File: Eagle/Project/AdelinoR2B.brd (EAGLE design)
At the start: 47 x 53.3 mm, 68 parts, among them J1 DC-044-A, J2 YELLOW-8P-2.54, J3 YELLOW-6P-2.54, J4 YELLOW-8P-2.54, J5 YELLOW-8P-2.54, J6 4P-2.0, J7 YELLOW-2X3P-2.54, J8 4P-2.0, Q1 NCE3407A, Q2 CJ2305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

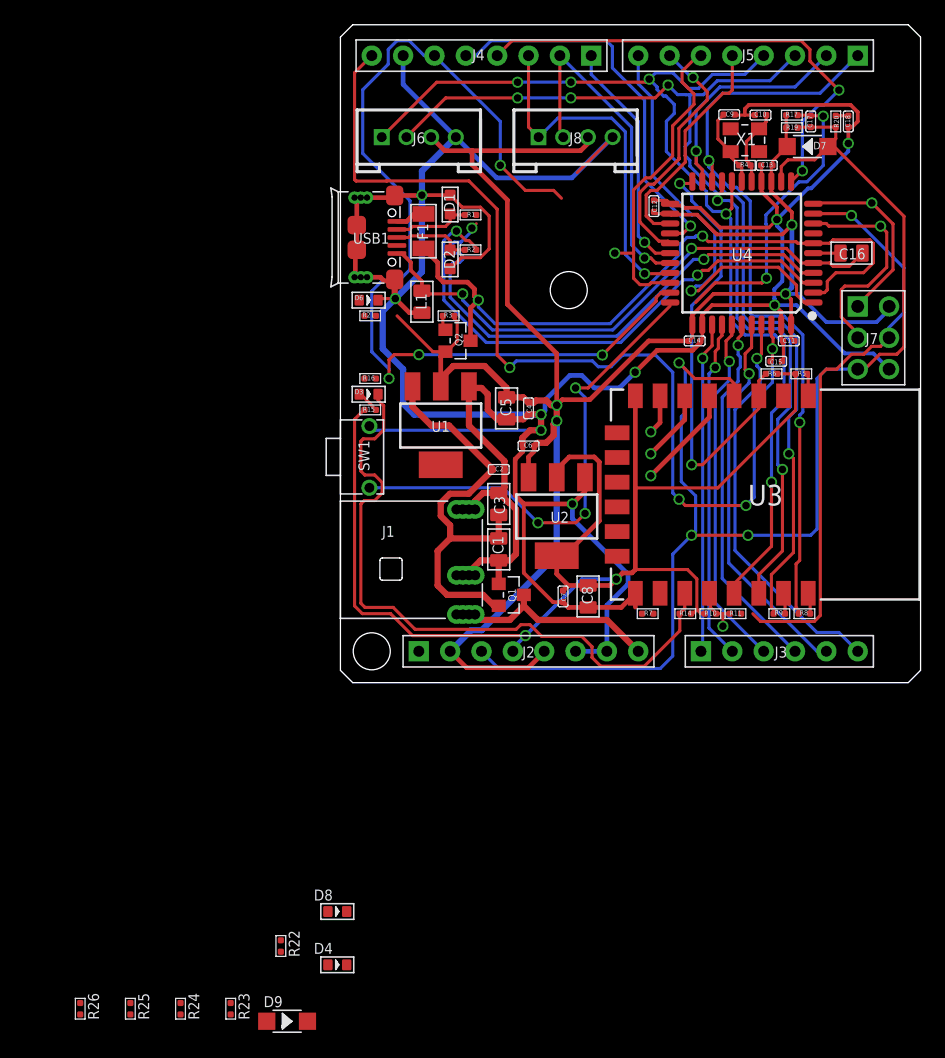
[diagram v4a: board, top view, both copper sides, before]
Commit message: Reserve resistor for GPIO16/RESET.
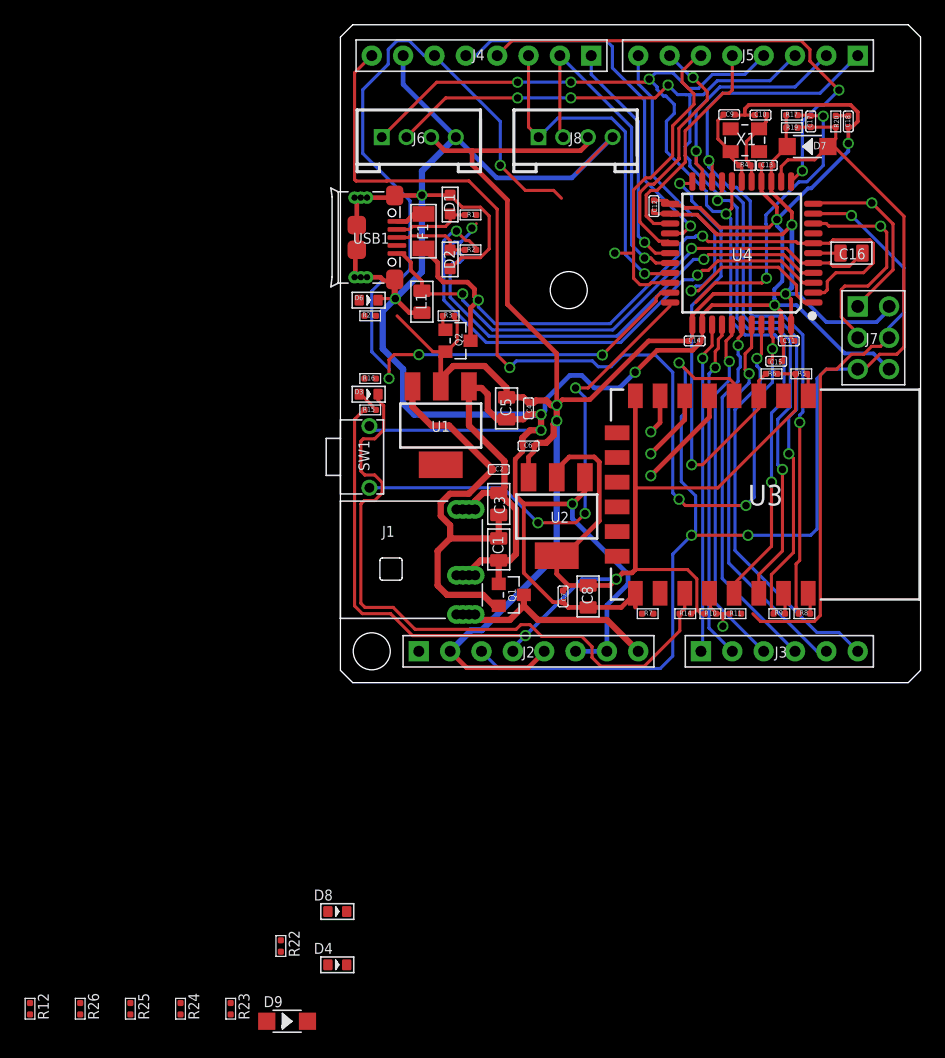
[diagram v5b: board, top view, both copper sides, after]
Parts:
- added R12: 0R, Seeed-Resistor:R0402
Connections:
- new net N$11: R12.2, U3.4
- net RESET: now also R12.1; no longer U3.4
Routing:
- net RESET: track 108.4 -> 107.4 mm
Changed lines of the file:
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@@
 <element name="C10" library="Seeed-Capacitor" package="C0402" value="22pf" x="34.036" y="45.9835" smashed="yes" rot="R90">
 <attribute name="MPN" value="CC0402JRNPO9BN220" x="34.036" y="45.9835" size="1.778" layer="27" rot="R90" display="off"/>
+<attribute name="NAME" x="33.528" y="45.8565" size="0.4064" layer="25" ratio="11"/>
 <attribute name="NAME" x="32.766" y="45.7295" size="0.635" layer="33" ratio="10"/>
-<attribute name="NAME" x="33.528" y="45.8565" size="0.4064" layer="25" ratio="11"/>
 <attribute name="VALUE" x="32.766" y="44.396" size="0.635" layer="27" ratio="10"/>
 </element>
@@
 <element name="C9" library="Seeed-Capacitor" package="C0402" value="22pf" x="31.496" y="46.0195" smashed="yes" rot="R270">
 <attribute name="MPN" value="CC0402JRNPO9BN220" x="31.496" y="46.0195" size="1.778" layer="27" rot="R270" display="off"/>
+<attribute name="NAME" x="31.877" y="46.2735" size="0.4064" layer="25" ratio="11" rot="R180"/>
 <attribute name="NAME" x="32.766" y="46.2735" size="0.635" layer="33" ratio="10" rot="R180"/>
-<attribute name="NAME" x="31.877" y="46.2735" size="0.4064" layer="25" ratio="11" rot="R180"/>
 <attribute name="VALUE" x="32.766" y="47.607" size="0.635" layer="27" ratio="10" rot="R180"/>
 </element>
@@
 <element name="J1" library="Seeed-Connector" package="DCJ3P-11.6X9.6X7.0MM" value="DC-044-A" x="0" y="9.906" smashed="yes" rot="R270">
 <attribute name="MPN" value="JACK-DC-044-A" x="0" y="9.906" size="1.778" layer="27" rot="R270" display="off"/>
+<attribute name="NAME" x="3.3655" y="11.811" size="0.889" layer="25" ratio="11"/>
 <attribute name="NAME" x="6.985" y="13.1445" size="1.27" layer="33" ratio="10" rot="R270"/>
-<attribute name="NAME" x="3.3655" y="11.811" size="0.889" layer="25" ratio="11"/>
 <attribute name="VALUE" x="4.3815" y="3.556" size="0.889" layer="27" ratio="11"/>
 </element>
 <element name="J3" library="Seeed-Connector" package="H6-2.54" value="YELLOW-6P-2.54" x="35.56" y="2.54" smashed="yes" rot="R90">
 <attribute name="MPN" value="F185-1106A1BSYA3" x="35.56" y="2.54" size="1.778" layer="27" rot="R90" display="off"/>
+<attribute name="NAME" x="36.195" y="2.921" size="0.889" layer="25" ratio="11" rot="R180"/>
 <attribute name="NAME" x="38.1" y="3.175" size="0.635" layer="33" ratio="10" rot="R180"/>
-<attribute name="NAME" x="36.195" y="2.921" size="0.889" layer="25" ratio="11" rot="R180"/>
 <attribute name="VALUE" x="37.465" y="5.08" size="0.889" layer="27" ratio="11" rot="R180"/>
 </element>
 <element name="J2" library="Seeed-Connector" package="H8-2.54" value="YELLOW-8P-2.54" x="15.24" y="2.54" smashed="yes" rot="R90">
 <attribute name="MPN" value="F185-1108A1BSYC1" x="15.24" y="2.54" size="1.778" layer="27" rot="R90" display="off"/>
+<attribute name="NAME" x="15.748" y="2.921" size="0.889" layer="25" ratio="11" rot="R180"/>
 <attribute name="NAME" x="15.875" y="2.54" size="0.3048" layer="33" ratio="10" rot="R180"/>
-<attribute name="NAME" x="15.748" y="2.921" size="0.889" layer="25" ratio="11" rot="R180"/>
 <attribute name="VALUE" x="16.51" y="5.08" size="0.889" layer="27" ratio="11" rot="R180"/>
 </element>
 <element name="J5" library="Seeed-Connector" package="H8-2.54" value="YELLOW-8P-2.54" x="33.02" y="50.8" smashed="yes" rot="R270">
 <attribute name="MPN" value="F185-1108A1BSYC1" x="33.02" y="50.8" size="1.778" layer="27" rot="R270" display="off"/>
+<attribute name="NAME" x="32.512" y="50.419" size="0.889" layer="25" ratio="11"/>
 <attribute name="NAME" x="32.385" y="50.8" size="0.3048" layer="33" ratio="10"/>
-<attribute name="NAME" x="32.512" y="50.419" size="0.889" layer="25" ratio="11"/>
 <attribute name="VALUE" x="31.75" y="48.26" size="0.889" layer="27" ratio="11"/>
 </element>
 <element name="J4" library="Seeed-Connector" package="H8-2.54" value="YELLOW-8P-2.54" x="11.43" y="50.8" smashed="yes" rot="R270">
 <attribute name="MPN" value="F185-1108A1BSYC1" x="11.43" y="50.8" size="1.778" layer="27" rot="R270" display="off"/>
+<attribute name="NAME" x="10.668" y="50.419" size="0.889" layer="25" ratio="11"/>
 <attribute name="NAME" x="10.795" y="50.8" size="0.3048" layer="33" ratio="10"/>
-<attribute name="NAME" x="10.668" y="50.419" size="0.889" layer="25" ratio="11"/>
 <attribute name="VALUE" x="10.16" y="48.26" size="0.889" layer="27" ratio="11"/>
 </element>
@@
 <element name="D9" library="Seeed-Diode" package="SOD-123" value="20V-500MA" x="-4.318" y="-27.432" smashed="yes">
 <attribute name="MPN" value="MBR0520LT1G" x="-4.318" y="-27.432" size="1.778" layer="27" display="off"/>
+<attribute name="NAME" x="-5.207" y="-28.067" size="0.381" layer="33" ratio="10"/>
 <attribute name="NAME" x="-6.223" y="-26.289" size="0.889" layer="25" ratio="11"/>
-<attribute name="NAME" x="-5.207" y="-28.067" size="0.381" layer="33" ratio="10"/>
 <attribute name="VALUE" x="-6.223" y="-29.464" size="0.889" layer="27" font="vector" ratio="11"/>
 </element>
@@
 <attribute name="NAME" x="-20.447" y="-25.146" size="0.889" layer="25" ratio="11" rot="R270"/>
 <attribute name="VALUE" x="-22.606" y="-25.146" size="0.889" layer="27" font="vector" ratio="11" rot="R270"/>
+</element>
+<element name="R12" library="Seeed-Resistor" package="R0402" value="0R" x="-25.146" y="-26.416" smashed="yes">
+<attribute name="MPN" value="RC0402JR-070RL" x="-25.146" y="-26.416" size="1.778" layer="27" display="off"/>
+<attribute name="NAME" x="-24.511" y="-25.146" size="0.889" layer="25" ratio="11" rot="R270"/>
+<attribute name="VALUE" x="-26.67" y="-25.146" size="0.889" layer="27" font="vector" ratio="11" rot="R270"/>
 </element>
 </elements>
@@
 <wire x1="43.69625" y1="26.6065" x2="42.48975" y2="25.4" width="0.254" layer="1"/>
 <wire x1="45.6565" y1="27.18625" x2="45.07675" y2="26.6065" width="0.254" layer="1"/>
-<contactref element="U3" pad="4"/>
 <wire x1="27.94" y1="25.4" x2="27.432" y2="25.908" width="0.254" layer="16"/>
 <via x="27.432" y="25.908" extent="1-16" drill="0.6096"/>
@@
 <wire x1="28.702" y1="24.638" x2="31.496" y2="24.638" width="0.254" layer="1"/>
 <wire x1="31.496" y1="24.638" x2="31.897" y2="24.237" width="0.254" layer="1"/>
-<wire x1="31.897" y1="24.237" x2="31.897" y2="23.24" width="0.254" layer="1"/>
+<contactref element="R12" pad="1"/>
+<wire x1="11.43" y1="2.54" x2="-25.146" y2="-25.9535" width="0" layer="19" extent="1-1"/>
 </signal>
 <signal name="PIN_AREF">
@@
 <wire x1="-1.016" y1="-22.86" x2="2.8755" y2="24.638" width="0" layer="19" extent="1-1"/>
 </signal>
+<signal name="N$11">
+<contactref element="U3" pad="4"/>
+<contactref element="R12" pad="2"/>
+<wire x1="-25.146" y1="-26.8785" x2="31.897" y2="23.24" width="0" layer="19" extent="1-1"/>
+</signal>
 </signals>

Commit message: Wip.
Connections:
- net +5V: no longer R16.1
- net GND: now also D4.-
- net PIN_D13: now also R16.1; no longer D4.-
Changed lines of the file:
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@@
 <element name="C10" library="Seeed-Capacitor" package="C0402" value="22pf" x="34.036" y="45.9835" smashed="yes" rot="R90">
 <attribute name="MPN" value="CC0402JRNPO9BN220" x="34.036" y="45.9835" size="1.778" layer="27" rot="R90" display="off"/>
+<attribute name="NAME" x="32.766" y="45.7295" size="0.635" layer="33" ratio="10"/>
 <attribute name="NAME" x="33.528" y="45.8565" size="0.4064" layer="25" ratio="11"/>
-<attribute name="NAME" x="32.766" y="45.7295" size="0.635" layer="33" ratio="10"/>
 <attribute name="VALUE" x="32.766" y="44.396" size="0.635" layer="27" ratio="10"/>
 </element>
@@
 <element name="C9" library="Seeed-Capacitor" package="C0402" value="22pf" x="31.496" y="46.0195" smashed="yes" rot="R270">
 <attribute name="MPN" value="CC0402JRNPO9BN220" x="31.496" y="46.0195" size="1.778" layer="27" rot="R270" display="off"/>
+<attribute name="NAME" x="32.766" y="46.2735" size="0.635" layer="33" ratio="10" rot="R180"/>
 <attribute name="NAME" x="31.877" y="46.2735" size="0.4064" layer="25" ratio="11" rot="R180"/>
-<attribute name="NAME" x="32.766" y="46.2735" size="0.635" layer="33" ratio="10" rot="R180"/>
 <attribute name="VALUE" x="32.766" y="47.607" size="0.635" layer="27" ratio="10" rot="R180"/>
 </element>
@@
 <element name="J1" library="Seeed-Connector" package="DCJ3P-11.6X9.6X7.0MM" value="DC-044-A" x="0" y="9.906" smashed="yes" rot="R270">
 <attribute name="MPN" value="JACK-DC-044-A" x="0" y="9.906" size="1.778" layer="27" rot="R270" display="off"/>
+<attribute name="NAME" x="6.985" y="13.1445" size="1.27" layer="33" ratio="10" rot="R270"/>
 <attribute name="NAME" x="3.3655" y="11.811" size="0.889" layer="25" ratio="11"/>
-<attribute name="NAME" x="6.985" y="13.1445" size="1.27" layer="33" ratio="10" rot="R270"/>
 <attribute name="VALUE" x="4.3815" y="3.556" size="0.889" layer="27" ratio="11"/>
 </element>
 <element name="J3" library="Seeed-Connector" package="H6-2.54" value="YELLOW-6P-2.54" x="35.56" y="2.54" smashed="yes" rot="R90">
 <attribute name="MPN" value="F185-1106A1BSYA3" x="35.56" y="2.54" size="1.778" layer="27" rot="R90" display="off"/>
+<attribute name="NAME" x="38.1" y="3.175" size="0.635" layer="33" ratio="10" rot="R180"/>
 <attribute name="NAME" x="36.195" y="2.921" size="0.889" layer="25" ratio="11" rot="R180"/>
-<attribute name="NAME" x="38.1" y="3.175" size="0.635" layer="33" ratio="10" rot="R180"/>
 <attribute name="VALUE" x="37.465" y="5.08" size="0.889" layer="27" ratio="11" rot="R180"/>
 </element>
 <element name="J2" library="Seeed-Connector" package="H8-2.54" value="YELLOW-8P-2.54" x="15.24" y="2.54" smashed="yes" rot="R90">
 <attribute name="MPN" value="F185-1108A1BSYC1" x="15.24" y="2.54" size="1.778" layer="27" rot="R90" display="off"/>
+<attribute name="NAME" x="15.875" y="2.54" size="0.3048" layer="33" ratio="10" rot="R180"/>
 <attribute name="NAME" x="15.748" y="2.921" size="0.889" layer="25" ratio="11" rot="R180"/>
-<attribute name="NAME" x="15.875" y="2.54" size="0.3048" layer="33" ratio="10" rot="R180"/>
 <attribute name="VALUE" x="16.51" y="5.08" size="0.889" layer="27" ratio="11" rot="R180"/>
 </element>
 <element name="J5" library="Seeed-Connector" package="H8-2.54" value="YELLOW-8P-2.54" x="33.02" y="50.8" smashed="yes" rot="R270">
 <attribute name="MPN" value="F185-1108A1BSYC1" x="33.02" y="50.8" size="1.778" layer="27" rot="R270" display="off"/>
+<attribute name="NAME" x="32.385" y="50.8" size="0.3048" layer="33" ratio="10"/>
 <attribute name="NAME" x="32.512" y="50.419" size="0.889" layer="25" ratio="11"/>
-<attribute name="NAME" x="32.385" y="50.8" size="0.3048" layer="33" ratio="10"/>
 <attribute name="VALUE" x="31.75" y="48.26" size="0.889" layer="27" ratio="11"/>
 </element>
 <element name="J4" library="Seeed-Connector" package="H8-2.54" value="YELLOW-8P-2.54" x="11.43" y="50.8" smashed="yes" rot="R270">
 <attribute name="MPN" value="F185-1108A1BSYC1" x="11.43" y="50.8" size="1.778" layer="27" rot="R270" display="off"/>
+<attribute name="NAME" x="10.795" y="50.8" size="0.3048" layer="33" ratio="10"/>
 <attribute name="NAME" x="10.668" y="50.419" size="0.889" layer="25" ratio="11"/>
-<attribute name="NAME" x="10.795" y="50.8" size="0.3048" layer="33" ratio="10"/>
 <attribute name="VALUE" x="10.16" y="48.26" size="0.889" layer="27" ratio="11"/>
 </element>
@@
 <element name="D9" library="Seeed-Diode" package="SOD-123" value="20V-500MA" x="-4.318" y="-27.432" smashed="yes">
 <attribute name="MPN" value="MBR0520LT1G" x="-4.318" y="-27.432" size="1.778" layer="27" display="off"/>
+<attribute name="NAME" x="-6.223" y="-26.289" size="0.889" layer="25" ratio="11"/>
 <attribute name="NAME" x="-5.207" y="-28.067" size="0.381" layer="33" ratio="10"/>
-<attribute name="NAME" x="-6.223" y="-26.289" size="0.889" layer="25" ratio="11"/>
 <attribute name="VALUE" x="-6.223" y="-29.464" size="0.889" layer="27" font="vector" ratio="11"/>
 </element>
@@
 <contactref element="D8" pad="-"/>
 <contactref element="R7" pad="1"/>
+<contactref element="D4" pad="-"/>
 <wire x1="3.175" y1="31.115" x2="3.048" y2="30.988" width="0" layer="19" extent="1-1"/>
 <wire x1="24.4295" y1="5.588" x2="23.897" y2="6.1205" width="0" layer="19" extent="1-1"/>
 <wire x1="0.508" y1="-18.542" x2="19.05" y2="2.54" width="0" layer="19" extent="1-1"/>
+<wire x1="0.508" y1="-22.86" x2="0.508" y2="-18.542" width="0" layer="19" extent="1-1"/>
 </signal>
 <signal name="N$1">
@@
 <wire x1="10.668" y1="41.956225" x2="10.668" y2="43.0975" width="0.381" layer="1"/>
 <contactref element="R21" pad="1"/>
-<contactref element="R16" pad="1"/>
 <wire x1="4.589" y1="29.718" x2="2.8755" y2="29.718" width="0" layer="19" extent="1-1"/>
-<wire x1="1.9505" y1="24.638" x2="2.8755" y2="29.718" width="0" layer="19" extent="1-1"/>
 <wire x1="8.128" y1="17.653" x2="8.128" y2="24.003" width="0" layer="19" extent="1-1"/>
 </signal>
@@
 <wire x1="17.272" y1="39.878" x2="17.907" y2="39.243" width="0.254" layer="1"/>
 <contactref element="R11" pad="2"/>
-<contactref element="D4" pad="-"/>
+<contactref element="R16" pad="1"/>
 <wire x1="21.2217625" y1="26.543" x2="32.4665" y2="5.588" width="0" layer="19" extent="1-1"/>
-<wire x1="0.508" y1="-22.86" x2="32.4665" y2="5.588" width="0" layer="19" extent="1-1"/>
+<wire x1="1.9505" y1="24.638" x2="3.937" y2="24.638" width="0" layer="19" extent="1-16"/>
 </signal>
 <signal name="PIN_D12">
